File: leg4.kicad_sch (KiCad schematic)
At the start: 12 parts, among them J11 Leg4 Motor1, J12 Leg4 Motor2, J13 Leg4 Motor3

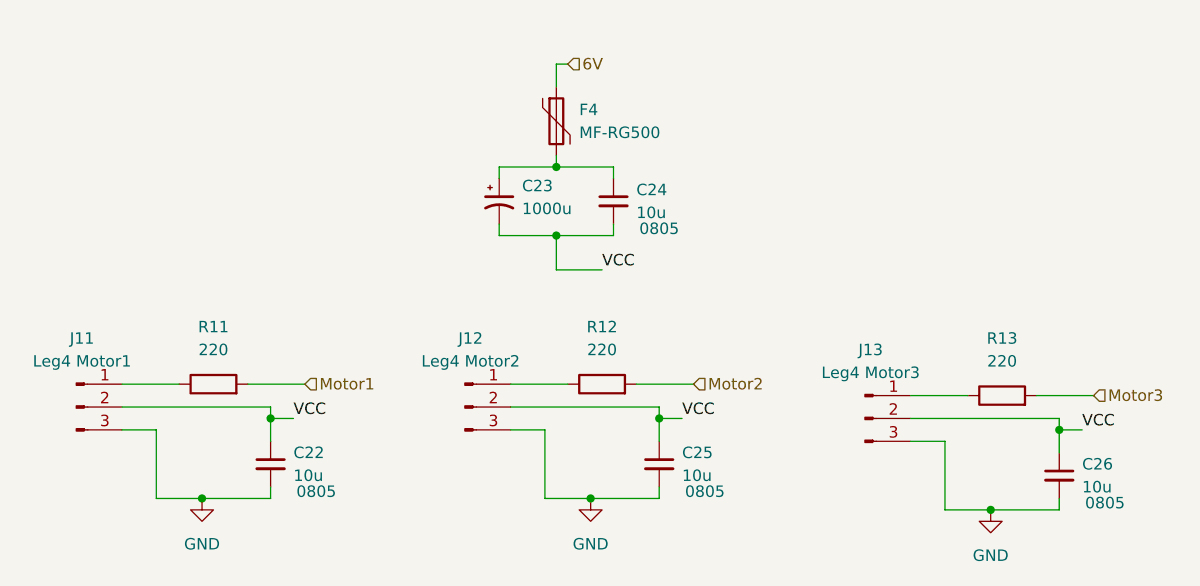
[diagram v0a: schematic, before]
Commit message: removed crystal, fixed caps
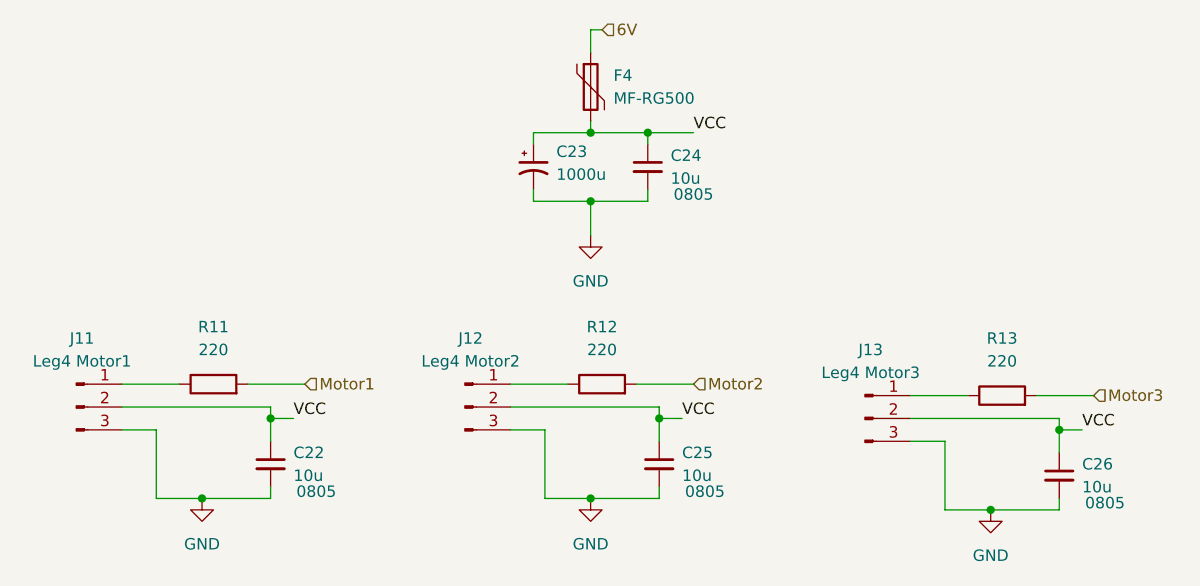
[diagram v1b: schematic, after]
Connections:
- net GND: now also C23.2, C24.2
- net VCC: now also C23.1, C24.1, F4.2; no longer C23.2, C24.2
